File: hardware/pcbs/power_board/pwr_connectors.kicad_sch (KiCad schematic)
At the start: 5 parts, among them J16 ScrewTerminal_02, J17 MTA100_02, J18 MTA100_02

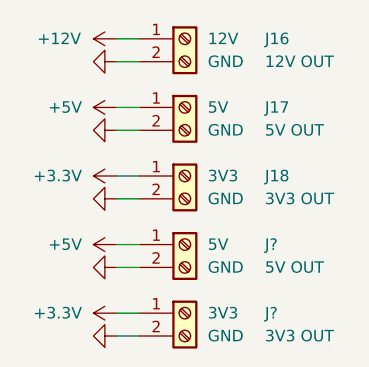
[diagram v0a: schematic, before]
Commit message: power_board: route USB3 connector
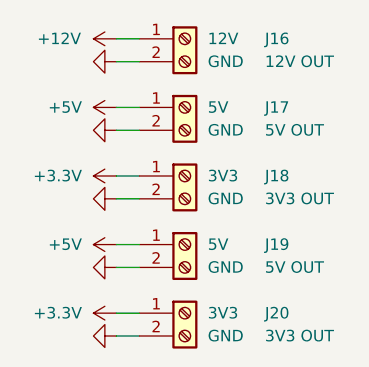
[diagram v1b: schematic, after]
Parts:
- gave numbers to parts that had none: 2
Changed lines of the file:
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@@
 		(dnp no)
 		(fields_autoplaced yes)
-		(property "Reference" "#PWR0104"
+		(property "Reference" "#PWR0105"
 			(at 139.7 104.14 0)
 			(effects
@@
 			(project "power_board"
 				(path "/4b166175-80a4-48c6-994d-6e62a6160b87/eb6931d2-84dc-4c44-a536-817b4a1688b3"
-					(reference "#PWR0104")
+					(reference "#PWR0105")
 					(unit 1)
 				)
@@
 		(dnp no)
 		(fields_autoplaced yes)
-		(property "Reference" "#PWR0101"
+		(property "Reference" "#PWR0102"
 			(at 129.54 91.44 0)
 			(effects
@@
 			(project "power_board"
 				(path "/4b166175-80a4-48c6-994d-6e62a6160b87/eb6931d2-84dc-4c44-a536-817b4a1688b3"
-					(reference "#PWR0101")
+					(reference "#PWR0102")
 					(unit 1)
 				)
@@
 		(dnp no)
 		(fields_autoplaced yes)
-		(property "Reference" "#PWR0102"
+		(property "Reference" "#PWR0103"
 			(at 139.7 96.52 0)
 			(effects
@@
 			(project "power_board"
 				(path "/4b166175-80a4-48c6-994d-6e62a6160b87/eb6931d2-84dc-4c44-a536-817b4a1688b3"
-					(reference "#PWR0102")
+					(reference "#PWR0103")
 					(unit 1)
 				)
@@
 		(on_board yes)
 		(dnp no)
-		(property "Reference" "J?"
+		(property "Reference" "J19"
 			(at 152.4 111.76 0)
 			(effects
@@
 			(project "power_board"
 				(path "/4b166175-80a4-48c6-994d-6e62a6160b87/eb6931d2-84dc-4c44-a536-817b4a1688b3"
-					(reference "J?")
+					(reference "J19")
 					(unit 1)
 				)
@@
 		(dnp no)
 		(fields_autoplaced yes)
-		(property "Reference" "#PWR0103"
+		(property "Reference" "#PWR0104"
 			(at 129.54 99.06 0)
 			(effects
@@
 			(project "power_board"
 				(path "/4b166175-80a4-48c6-994d-6e62a6160b87/eb6931d2-84dc-4c44-a536-817b4a1688b3"
-					(reference "#PWR0103")
+					(reference "#PWR0104")
 					(unit 1)
 				)
@@
 		(dnp no)
 		(fields_autoplaced yes)
-		(property "Reference" "#PWR0105"
+		(property "Reference" "#PWR0106"
 			(at 129.54 106.68 0)
 			(effects
@@
 			(project "power_board"
 				(path "/4b166175-80a4-48c6-994d-6e62a6160b87/eb6931d2-84dc-4c44-a536-817b4a1688b3"
-					(reference "#PWR0105")
+					(reference "#PWR0106")
 					(unit 1)
 				)
@@
 		(on_board yes)
 		(dnp no)
-		(property "Reference" "#PWR0100"
+		(property "Reference" "#PWR0101"
 			(at 139.7 88.9 0)
 			(effects
@@
 			(project "power_board"
 				(path "/4b166175-80a4-48c6-994d-6e62a6160b87/eb6931d2-84dc-4c44-a536-817b4a1688b3"
-					(reference "#PWR0100")
+					(reference "#PWR0101")
 					(unit 1)
 				)
@@
 		(on_board yes)
 		(dnp no)
-		(property "Reference" "J?"
+		(property "Reference" "J20"
 			(at 152.4 119.38 0)
 			(effects
@@
 			(project "power_board"
 				(path "/4b166175-80a4-48c6-994d-6e62a6160b87/eb6931d2-84dc-4c44-a536-817b4a1688b3"
-					(reference "J?")
-					(unit 1)
-				)
+					(reference "J20")
+					(unit 1)
+				)

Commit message: power_board: final-ish shape
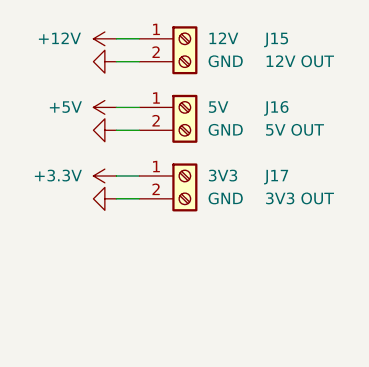
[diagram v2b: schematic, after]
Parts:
- removed J18: MTA100_02, conn:TerminalBlock_4Ucon_1x02_P3.50mm_Vertical, symbol conn:Screw_Terminal_01x02
- removed J19: MTA100_02, Connector_MTA-100:mta100_01x2_P2.54_647050-2, symbol conn:Screw_Terminal_01x02
- J17: renamed from J20; footprint conn:TerminalBlock_4Ucon_1x02_P3.50mm_Vertical -> Connector_MTA-100:mta100_01x2_P2.54_647050-2
- renumbered J16 to J15, J17 to J16
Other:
- moved on the sheet: J17

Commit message: power_board: use purpose labels on connectors
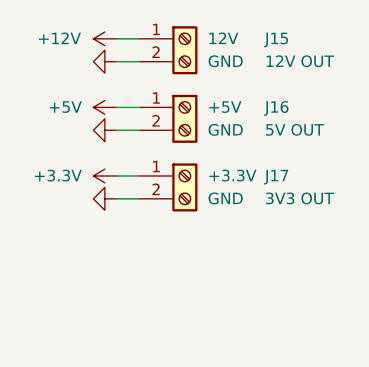
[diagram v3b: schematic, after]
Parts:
- J16: Purpose Pin1 5V -> +5V
- J17: Purpose Pin1 3V3 -> +3.3V
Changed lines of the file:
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@@
 			)
 		)
-		(property "Purpose Pin1" "3V3"
+		(property "Purpose Pin1" "+3.3V"
 			(at 146.05 104.14 0)
 			(effects
@@
 			)
 		)
-		(property "Purpose Pin1" "5V"
+		(property "Purpose Pin1" "+5V"
 			(at 146.05 96.52 0)
 			(effects

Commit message: pcbs: update purchase info
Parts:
- J15: Part 15EDGVC-3.5-02P-14-00AH and 15EDGKA-3.5-02P-14-100AH -> 15EDGVC-3.5-02P-14-00AH, 15EDGKA-3.5-02P-14-100AH
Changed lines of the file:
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@@
 			)
 		)
-		(property "Part" "15EDGVC-3.5-02P-14-00AH and 15EDGKA-3.5-02P-14-100AH"
+		(property "Part" "15EDGVC-3.5-02P-14-00AH, 15EDGKA-3.5-02P-14-100AH"
 			(at 143.51 88.9 0)
 			(effects

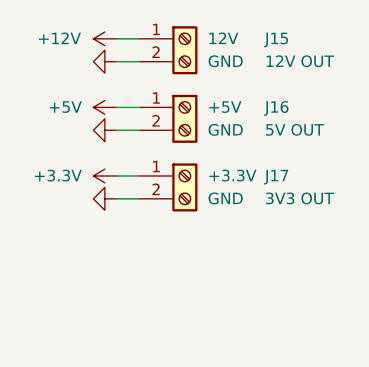
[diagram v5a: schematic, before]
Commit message: power_board: flip 12V connectors
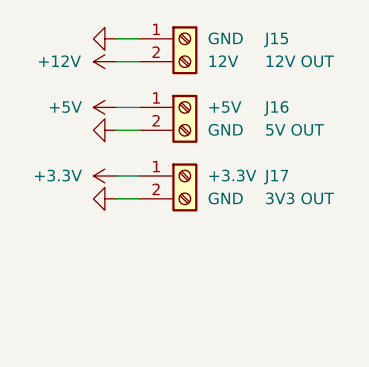
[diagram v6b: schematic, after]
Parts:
- J15: Purpose Pin1 12V -> GND; Purpose Pin2 GND -> 12V
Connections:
- net +12V: now also J15.2 (Pin_2); no longer J15.1 (Pin_1)
- net GND: now also J15.1 (Pin_1); no longer J15.2 (Pin_2)
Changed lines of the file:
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@@
+	(wire
+		(pts
+			(xy 135.89 91.44) (xy 138.43 91.44)
+		)
+		(stroke
+			(width 0)
+			(type default)
+		)
+	)
+	(wire
+		(pts
+			(xy 138.43 104.14) (xy 135.89 104.14)
+		)
+		(stroke
+			(width 0)
+			(type default)
+		)
+	)
 	(wire
 		(pts
 			(xy 135.89 88.9) (xy 138.43 88.9)
-		)
-		(stroke
-			(width 0)
-			(type default)
-		)
-	)
-	(wire
-		(pts
-			(xy 138.43 104.14) (xy 135.89 104.14)
-		)
-		(stroke
-			(width 0)
-			(type default)
-		)
-	)
-	(wire
-		(pts
-			(xy 135.89 91.44) (xy 138.43 91.44)
 		)
 		(stroke
@@
 	(symbol
 		(lib_id "power:GND")
-		(at 135.89 91.44 270)
+		(at 135.89 88.9 270)
+		(mirror x)
 		(unit 1)
 		(exclude_from_sim no)
@@
 		(fields_autoplaced yes)
 		(property "Reference" "#PWR0102"
-			(at 129.54 91.44 0)
+			(at 129.54 88.9 0)
 			(effects
 				(font
@@
 		)
 		(property "Value" "GND"
-			(at 130.81 91.44 0)
+			(at 130.81 88.9 0)
 			(effects
 				(font
@@
 		)
 		(property "Footprint" ""
-			(at 135.89 91.44 0)
+			(at 135.89 88.9 0)
 			(effects
 				(font
@@
 		)
 		(property "Datasheet" ""
-			(at 135.89 91.44 0)
-			(effects
-				(font
-					(size 1.27 1.27)
-				)
-				(hide yes)
-			)
-		)
-		(property "Description" ""
-			(at 135.89 91.44 0)
+			(at 135.89 88.9 0)
+			(effects
+				(font
+					(size 1.27 1.27)
+				)
+				(hide yes)
+			)
+		)
+		(property "Description" ""
+			(at 135.89 88.9 0)
 			(effects
 				(font
@@
 			)
 		)
-		(property "Purpose Pin1" "12V"
+		(property "Purpose Pin1" "GND"
 			(at 146.05 88.9 0)
 			(effects
@@
 			)
 		)
-		(property "Purpose Pin2" "GND"
+		(property "Purpose Pin2" "12V"
 			(at 146.05 91.44 0)
 			(effects
@@
 	(symbol
 		(lib_id "power:+12V")
-		(at 135.89 88.9 90)
+		(at 135.89 91.44 90)
+		(mirror x)
 		(unit 1)
 		(exclude_from_sim no)
@@
 		(dnp no)
 		(property "Reference" "#PWR0101"
-			(at 139.7 88.9 0)
+			(at 139.7 91.44 0)
 			(effects
 				(font
@@
 		)
 		(property "Value" "+12V"
-			(at 129.54 88.9 90)
+			(at 129.54 91.44 90)
 			(effects
 				(font
@@
 		)
 		(property "Footprint" ""
-			(at 135.89 88.9 0)
+			(at 135.89 91.44 0)
 			(effects
 				(font
@@
 		)
 		(property "Datasheet" ""
-			(at 135.89 88.9 0)
-			(effects
-				(font
-					(size 1.27 1.27)
-				)
-				(hide yes)
-			)
-		)
-		(property "Description" ""
-			(at 135.89 88.9 0)
-			(effects
-				(font
+			(at 135.89 91.44 0)
+			(effects
+				(font
+					(size 1.27 1.27)
+				)
+				(hide yes)
+			)
+		)
+		(property "Description" ""
+			(at 135.89 91.44 0)
+			(effects
+				(font

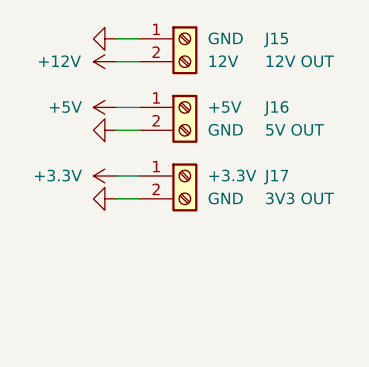
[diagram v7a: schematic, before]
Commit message: power_board: axe one fan output to make space for caps
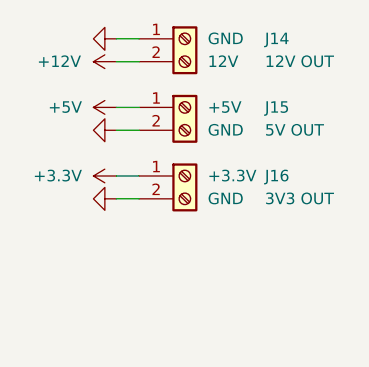
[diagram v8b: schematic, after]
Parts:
- renumbered J15 to J14, J16 to J15, J17 to J16
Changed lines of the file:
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@@
 		(dnp no)
 		(fields_autoplaced yes)
-		(property "Reference" "#PWR0105"
+		(property "Reference" "#PWR0103"
 			(at 139.7 104.14 0)
 			(effects
@@
 			(project "power_board"
 				(path "/4b166175-80a4-48c6-994d-6e62a6160b87/eb6931d2-84dc-4c44-a536-817b4a1688b3"
-					(reference "#PWR0105")
+					(reference "#PWR0103")
 					(unit 1)
 				)
@@
 		(dnp no)
 		(fields_autoplaced yes)
-		(property "Reference" "#PWR0101"
+		(property "Reference" "#PWR099"
 			(at 129.54 88.9 0)
 			(effects
@@
 			(project "power_board"
 				(path "/4b166175-80a4-48c6-994d-6e62a6160b87/eb6931d2-84dc-4c44-a536-817b4a1688b3"
-					(reference "#PWR0101")
+					(reference "#PWR099")
 					(unit 1)
 				)
@@
 		(dnp no)
 		(fields_autoplaced yes)
-		(property "Reference" "#PWR0103"
+		(property "Reference" "#PWR0101"
 			(at 139.7 96.52 0)
 			(effects
@@
 			(project "power_board"
 				(path "/4b166175-80a4-48c6-994d-6e62a6160b87/eb6931d2-84dc-4c44-a536-817b4a1688b3"
-					(reference "#PWR0103")
+					(reference "#PWR0101")
 					(unit 1)
 				)
@@
 		(dnp no)
 		(fields_autoplaced yes)
-		(property "Reference" "#PWR0104"
+		(property "Reference" "#PWR0102"
 			(at 129.54 99.06 0)
 			(effects
@@
 			(project "power_board"
 				(path "/4b166175-80a4-48c6-994d-6e62a6160b87/eb6931d2-84dc-4c44-a536-817b4a1688b3"
-					(reference "#PWR0104")
+					(reference "#PWR0102")
 					(unit 1)
 				)
@@
 		(dnp no)
 		(fields_autoplaced yes)
-		(property "Reference" "#PWR0106"
+		(property "Reference" "#PWR0104"
 			(at 129.54 106.68 0)
 			(effects
@@
 			(project "power_board"
 				(path "/4b166175-80a4-48c6-994d-6e62a6160b87/eb6931d2-84dc-4c44-a536-817b4a1688b3"
-					(reference "#PWR0106")
+					(reference "#PWR0104")
 					(unit 1)
 				)
@@
 		(on_board yes)
 		(dnp no)
-		(property "Reference" "J15"
+		(property "Reference" "J14"
 			(at 152.4 88.9 0)
 			(effects
@@
 			(project "power_board"
 				(path "/4b166175-80a4-48c6-994d-6e62a6160b87/eb6931d2-84dc-4c44-a536-817b4a1688b3"
-					(reference "J15")
+					(reference "J14")
 					(unit 1)
 				)
@@
 		(on_board yes)
 		(dnp no)
-		(property "Reference" "#PWR0102"
+		(property "Reference" "#PWR0100"
 			(at 139.7 91.44 0)
 			(effects
@@
 			(project "power_board"
 				(path "/4b166175-80a4-48c6-994d-6e62a6160b87/eb6931d2-84dc-4c44-a536-817b4a1688b3"
-					(reference "#PWR0102")
+					(reference "#PWR0100")
 					(unit 1)
 				)
@@
 		(on_board yes)
 		(dnp no)
-		(property "Reference" "J17"
+		(property "Reference" "J16"
 			(at 152.4 104.14 0)
 			(effects
@@
 			(project "power_board"
 				(path "/4b166175-80a4-48c6-994d-6e62a6160b87/eb6931d2-84dc-4c44-a536-817b4a1688b3"
-					(reference "J17")
+					(reference "J16")
 					(unit 1)
 				)
@@
 		(on_board yes)
 		(dnp no)
-		(property "Reference" "J16"
+		(property "Reference" "J15"
 			(at 152.4 96.52 0)
 			(effects
@@
 			(project "power_board"
 				(path "/4b166175-80a4-48c6-994d-6e62a6160b87/eb6931d2-84dc-4c44-a536-817b4a1688b3"
-					(reference "J16")
-					(unit 1)
-				)
+					(reference "J15")
+					(unit 1)
+				)
